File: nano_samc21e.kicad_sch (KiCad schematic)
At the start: 31 parts, among them J2 Castellated_headers, SW1 RST, U1 ATSAMC21E18A-M, U2 AP2112K-3.3, U3 LMZM23600V5, Y1 32.768kHz

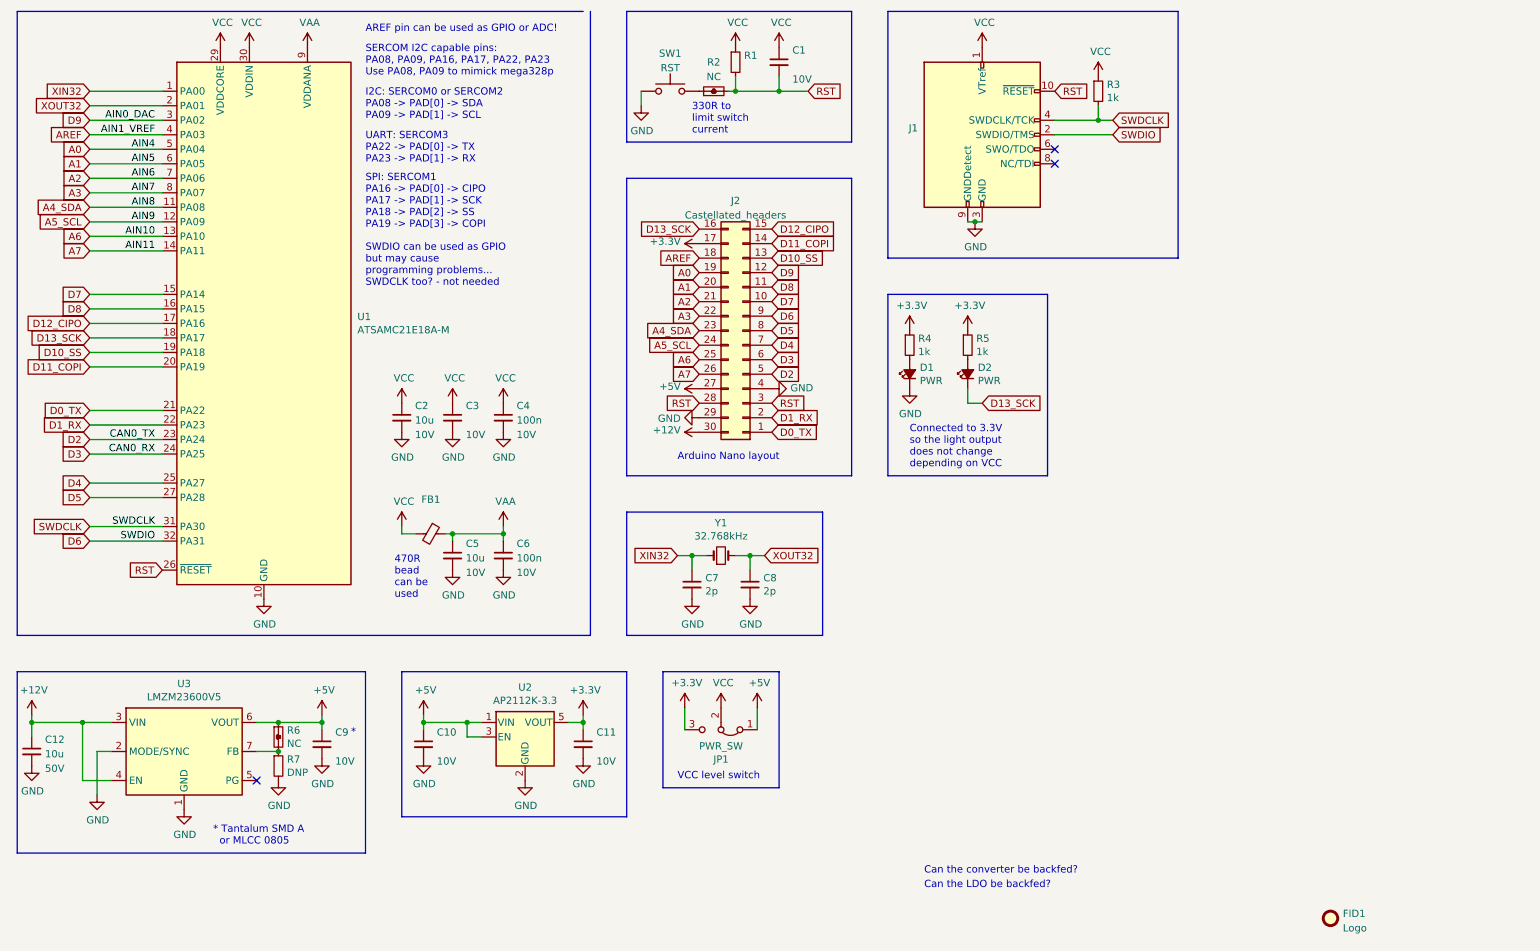
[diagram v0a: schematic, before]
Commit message: Massive rework: - 2 layer PCB - design restraints set according to JLCPCB capabilites - no castellated holes, smaller board dimensions - Arduino style numbering on top silkscreen - Changed footprints to match JLCPCB basic parts TODO: layout and routing
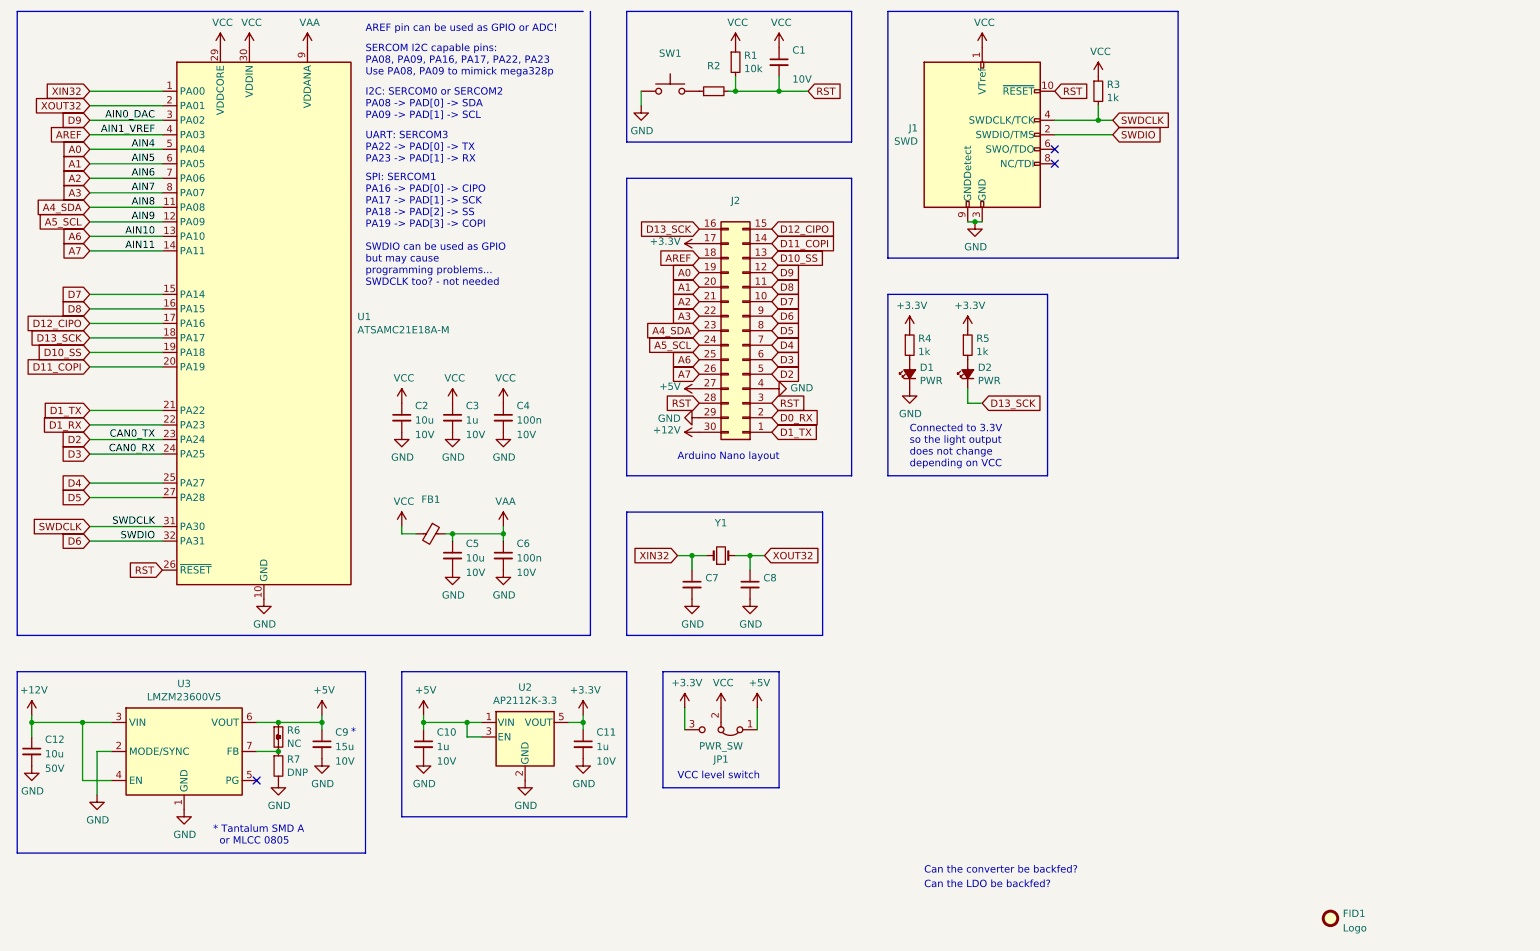
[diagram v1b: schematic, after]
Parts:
- C10, C11, C3: value (none) -> 1u
- C7, C8: value 2p -> (none)
- C9: value (none) -> 15u; footprint (none) -> Capacitor_SMD:C_1206_3216Metric
- J1: value (none) -> SWD; footprint (none) -> Connector_PinHeader_1.27mm:PinHeader_2x05_P1.27mm_Vertical_SMD
- J2: value Castellated_headers -> (none); footprint global:Arduino_Nano_castellated -> (none)
- R1: value (none) -> 10k
- R2: value NC -> (none); footprint global:0402_NC_minimalist -> (none); symbol global:R_Small_NC -> Device:R_Small
- SW1: value RST -> (none); footprint global:SW_Push_Alps_SKRK -> (none)
- Y1: value 32.768kHz -> (none); footprint Crystal:Crystal_SMD_2012-2Pin_2.0x1.2mm -> (none)
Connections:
- net D1_RX: no longer J2.2 (Pin_2)
- net D0_TX renamed D1_TX
- new net D0_RX: J2.2 (Pin_2)
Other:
- note removed: "330R to limit switch current"
- note removed: "470R bead can be used"

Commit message: v1.0 finished - layout and routing finished - added front and back graphics, JLCPCB tooling holes
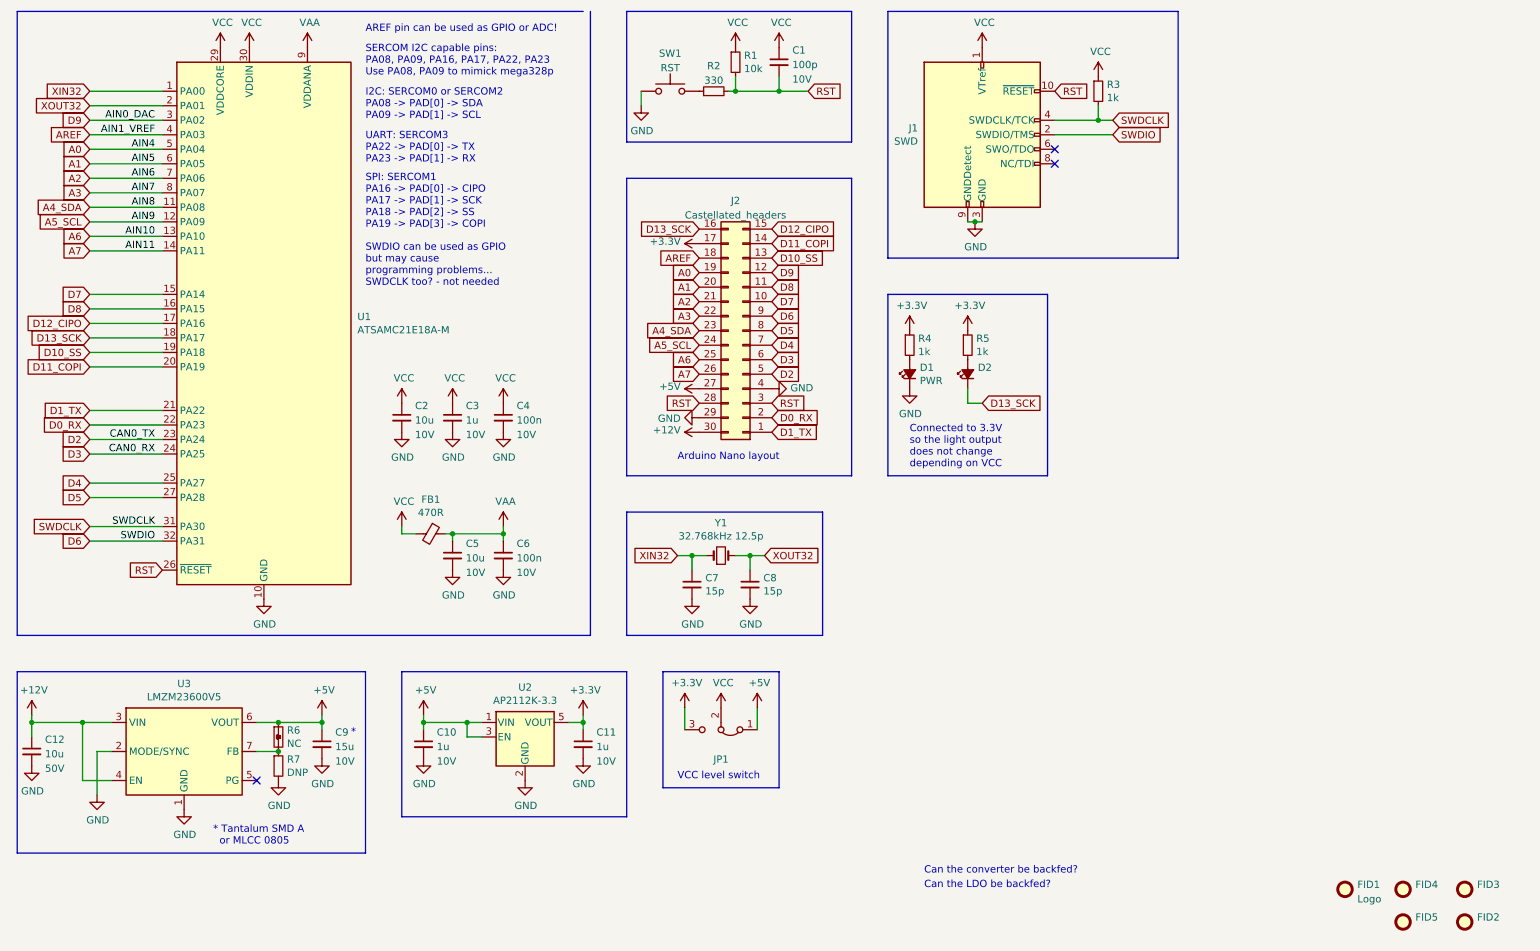
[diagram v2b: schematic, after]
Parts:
- added FID2, FID3, FID4, FID5: (no value), symbol Mechanical:Fiducial
- C1: value (none) -> 100p; footprint (none) -> global:0402_minimalist
- C10, C11, C3, R1, R3, R4, R5: footprint (none) -> global:0402_minimalist
- C7, C8: value (none) -> 15p
- D2: value PWR -> (none)
- FB1: value (none) -> 470R; footprint (none) -> global:0603_minimalist
- J2: value (none) -> Castellated_headers; footprint (none) -> global:Arduino_Nano
- JP1: value PWR_SW -> (none); footprint global:0603_3pos_jumper -> (none)
- R2: value (none) -> 330; footprint (none) -> global:0402_minimalist
- SW1: value (none) -> RST; footprint (none) -> Button_Switch_SMD:SW_SPST_SKQG_WithStem
- Y1: value (none) -> 32.768kHz 12.5p; footprint (none) -> Crystal:Crystal_SMD_3215-2Pin_3.2x1.5mm
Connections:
- net D1_RX is gone; now on net D0_RX: U1.22 (PA23)
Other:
- moved on the sheet: FID1

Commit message: Added missing pin numbering Added WEEE logo Added JLCPCB order number Generated fresh JLCPCB output files
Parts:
- added FID6: (no value), symbol Mechanical:Fiducial
- D2: value (none) -> USER
- FID2, FID3: value (none) -> Tooling; footprint (none) -> global:JLCPCB_tooling_hole
- FID4: value (none) -> Logo2; footprint (none) -> global:turboino_logo
- FID5: value (none) -> Logo3; footprint (none) -> global:turboino_back
- JP1: value (none) -> PWR_SW; footprint (none) -> Connector_PinHeader_2.54mm:PinHeader_1x03_P2.54mm_Vertical
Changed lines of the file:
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@@
     (in_bom yes) (on_board yes)
     (property "Reference" "JP1" (id 0) (at 142.24 148.6916 0))
-    (property "Value" "" (id 1) (at 142.24 146.3802 0))
-    (property "Footprint" "" (id 2) (at 142.24 143.51 0)
+    (property "Value" "PWR_SW" (id 1) (at 142.24 146.3802 0))
+    (property "Footprint" "Connector_PinHeader_2.54mm:PinHeader_1x03_P2.54mm_Vertical" (id 2) (at 142.24 143.51 0)
       (effects (font (size 1.27 1.27)) hide)
     )
@@
     (pin "2")
   )
+  (symbol (lib_id "Mechanical:Fiducial") (at 251.46 177.165 0) (unit 1)
+    (in_bom yes) (on_board yes) (fields_autoplaced)
+    (property "Reference" "FID6" (id 0) (at 253.619 176.3303 0)
+      (effects (font (size 1.27 1.27)) (justify left))
+    )
+    (property "Value" "" (id 1) (at 253.619 178.8672 0)
+      (effects (font (size 1.27 1.27)) (justify left))
+    )
+    (property "Footprint" "" (id 2) (at 251.46 177.165 0)
+      (effects (font (size 1.27 1.27)) hide)
+    )
+    (property "Datasheet" "~" (id 3) (at 251.46 177.165 0)
+      (effects (font (size 1.27 1.27)) hide)
+    )
+  )
   (symbol (lib_id "Device:C_Small") (at 90.17 146.05 0) (unit 1)
     (in_bom yes) (on_board yes)
@@
       (effects (font (size 1.27 1.27)) (justify left))
     )
-    (property "Value" "" (id 1) (at 263.779 178.8672 0)
-      (effects (font (size 1.27 1.27)) (justify left))
-    )
-    (property "Footprint" "" (id 2) (at 261.62 177.165 0)
+    (property "Value" "Logo3" (id 1) (at 263.779 178.8672 0)
+      (effects (font (size 1.27 1.27)) (justify left))
+    )
+    (property "Footprint" "global:turboino_back" (id 2) (at 261.62 177.165 0)
       (effects (font (size 1.27 1.27)) hide)
     )
@@
       (effects (font (size 1.27 1.27)) (justify right))
     )
-    (property "Value" "" (id 1) (at 187.198 82.423 90)
+    (property "Value" "USER" (id 1) (at 187.198 82.423 90)
       (effects (font (size 1.27 1.27)) (justify right))
     )
@@
       (effects (font (size 1.27 1.27)) (justify left))
     )
-    (property "Value" "" (id 1) (at 274.574 173.1522 0)
-      (effects (font (size 1.27 1.27)) (justify left))
-    )
-    (property "Footprint" "" (id 2) (at 272.415 171.45 0)
+    (property "Value" "Tooling" (id 1) (at 274.574 173.1522 0)
+      (effects (font (size 1.27 1.27)) (justify left))
+    )
+    (property "Footprint" "global:JLCPCB_tooling_hole" (id 2) (at 272.415 171.45 0)
       (effects (font (size 1.27 1.27)) hide)
     )
@@
       (effects (font (size 1.27 1.27)) (justify left))
     )
-    (property "Value" "" (id 1) (at 274.574 178.8672 0)
-      (effects (font (size 1.27 1.27)) (justify left))
-    )
-    (property "Footprint" "" (id 2) (at 272.415 177.165 0)
+    (property "Value" "Tooling" (id 1) (at 274.574 178.8672 0)
+      (effects (font (size 1.27 1.27)) (justify left))
+    )
+    (property "Footprint" "global:JLCPCB_tooling_hole" (id 2) (at 272.415 177.165 0)
       (effects (font (size 1.27 1.27)) hide)
     )
@@
       (effects (font (size 1.27 1.27)) (justify left))
     )
-    (property "Value" "" (id 1) (at 263.779 173.1522 0)
-      (effects (font (size 1.27 1.27)) (justify left))
-    )
-    (property "Footprint" "" (id 2) (at 261.62 171.45 0)
+    (property "Value" "Logo2" (id 1) (at 263.779 173.1522 0)
+      (effects (font (size 1.27 1.27)) (justify left))
+    )
+    (property "Footprint" "global:turboino_logo" (id 2) (at 261.62 171.45 0)
       (effects (font (size 1.27 1.27)) hide)
     )
@@
       (reference "FID5") (unit 1) (value "Logo3") (footprint "global:turboino_back")
     )
+    (path "/0976ae08-39c8-474c-be26-5628b6c436bc"
+      (reference "FID6") (unit 1) (value "WEEE") (footprint "Symbol:WEEE-Logo_4.2x6mm_SilkScreen")
+    )
     (path "/00000000-0000-0000-0000-000062685ec0"
